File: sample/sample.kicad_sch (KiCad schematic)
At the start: 40 parts, among them M1 NMOS4pin, M2 PMOS4pin, M3 NMOS4pin, M4 PMOS4pin, M5 NMOS4pin, M6 PMOS4pin, M7 NMOS4pin, M8 NMOS4pin, M9 NMOS3pin_1, U1 GND_Drafting, U10 not, U11 V_{DD}, U12 D_FF_R, U13 nor21, U14 D_FF_R, U15 D_FF_R, U16 nor21, U17 D_FF_R, U18 D_FF_R, U19 OP_AMP, U2 V_{DD}, U20 delay, U21 OP_AMP, U22 RS_FF, U25 nand21, U3 V_{DD}, U4 GND_Drafting, U5 GND_Drafting, U6 GND_Drafting, U7 V_{DD}, U8 V_{DD}, U9 or31

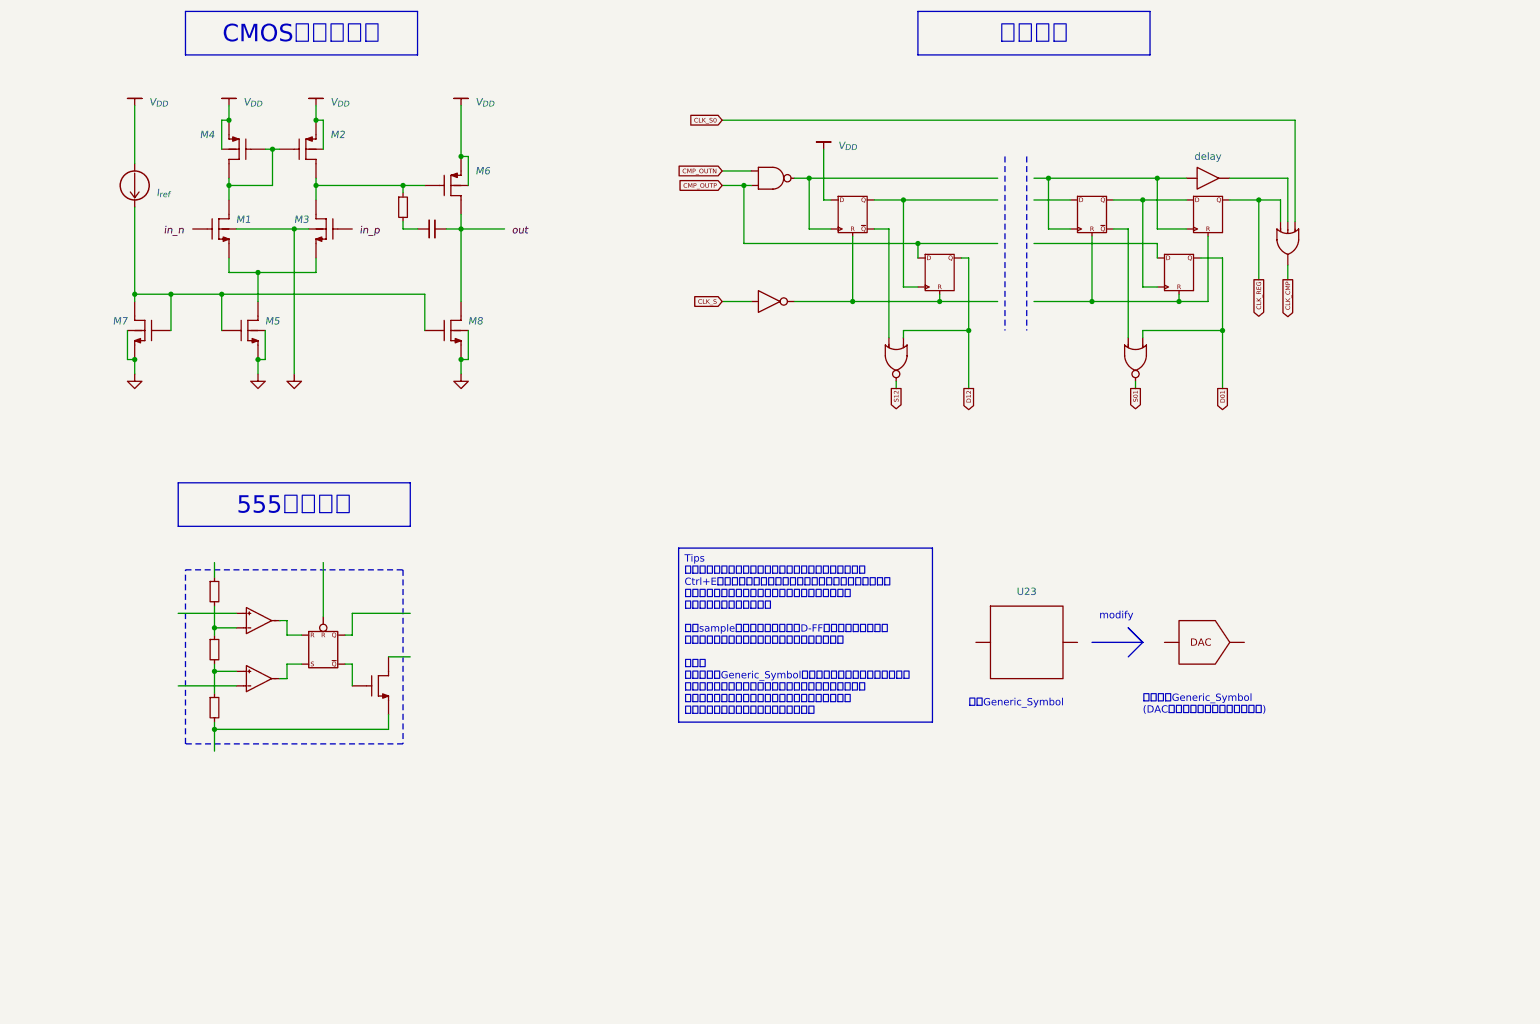
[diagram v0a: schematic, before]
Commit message: マルチプレクサの追加とサンプルの改修
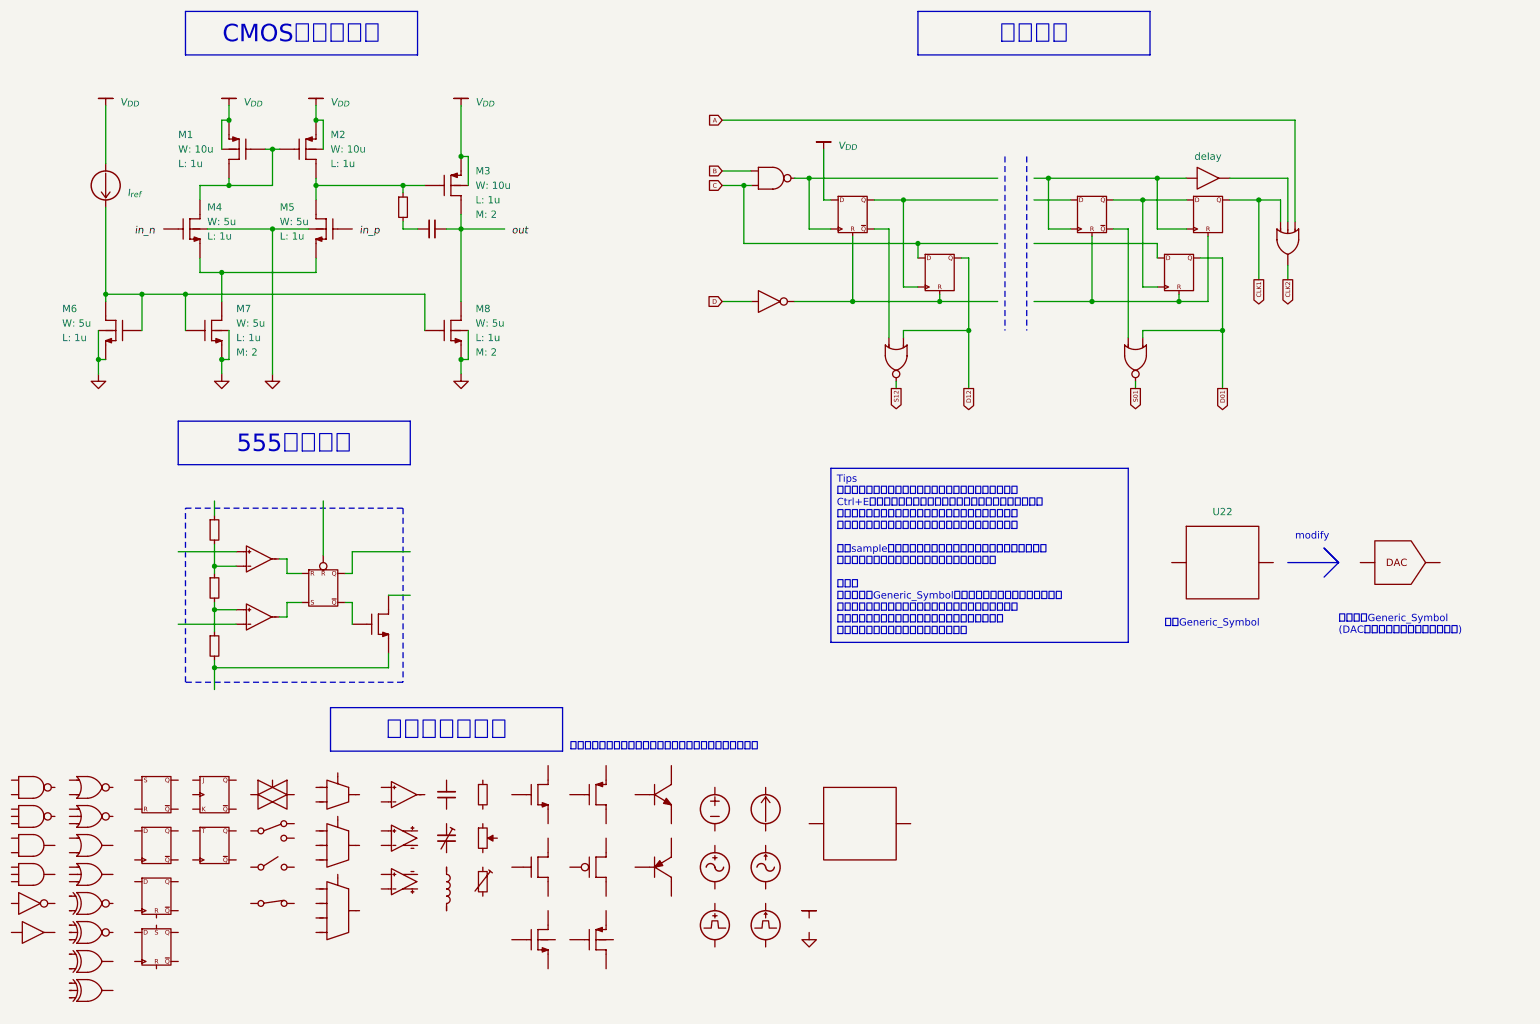
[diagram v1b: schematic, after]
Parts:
- removed M1, M3: NMOS4pin, symbol Drafting_Symbols:NMOS4pin
- removed M4, M6: PMOS4pin, symbol Drafting_Symbols:PMOS4pin
- added C2: C, symbol Drafting_Symbols:C_Drafting
- added C3: C_Trim, symbol Drafting_Symbols:C_Trim_Drafting
- added I_AC1: I_AC, symbol Drafting_Symbols:I_AC
- added I_DC2: I_DC, symbol Drafting_Symbols:I_DC
- added I_Pulse1: I_Pulse, symbol Drafting_Symbols:I_Pulse
- added L1: L, symbol Drafting_Symbols:L_Drafting
- added M1, M15, M3: PMOS4pin, symbol Drafting_Symbols:PMOS4pin
- added M10: NMOS3pin_1, symbol Drafting_Symbols:NMOS3pin_1
- added M11: PMOS3pin_1, symbol Drafting_Symbols:PMOS3pin_1
- added M12: NMOS3pin_2, symbol Drafting_Symbols:NMOS3pin_2
- added M13: PMOS3pin_2, symbol Drafting_Symbols:PMOS3pin_2
- added M14, M4, M6: NMOS4pin, symbol Drafting_Symbols:NMOS4pin
- added Q1: NPN, symbol Drafting_Symbols:NPN
- added Q2: PNP, symbol Drafting_Symbols:PNP
- added R5: R, symbol Drafting_Symbols:R_Drafting
- added R6: R, symbol Drafting_Symbols:R_Trim_Drafting
- added RV1: R_POT, symbol Drafting_Symbols:R_Potentiometer_Drafting
- added SW1: SW_CMOS, symbol Drafting_Symbols:SW_CMOS
- added SW2: SW_SPDT, symbol Drafting_Symbols:SW_SPDT
- added SW3: SW_SPST_OFF, symbol Drafting_Symbols:SW_SPST_OFF
- added SW4: SW_SPST_ON, symbol Drafting_Symbols:SW_SPST_ON
- added U26: nand21, symbol Drafting_Symbols:nand21
- added U27: nor21, symbol Drafting_Symbols:nor21
- added U28: RS_FF, symbol Drafting_Symbols:RS_FF
- added U29: JK_FF, symbol Drafting_Symbols:JK_FF
- added U30: MUX21, symbol Drafting_Symbols:MUX21
- added U31: OP_AMP, symbol Drafting_Symbols:OP_AMP
- added U32: nand31, symbol Drafting_Symbols:nand31
- added U33: nor31, symbol Drafting_Symbols:nor31
- added U34: ~, symbol Drafting_Symbols:Generic_Symbol
- added U35: Differential_AMP, symbol Drafting_Symbols:Differential_AMP_2
- added U36: and21, symbol Drafting_Symbols:and21
- added U37: or21, symbol Drafting_Symbols:or21
- added U38: D_FF, symbol Drafting_Symbols:D_FF
- added U39: T_FF, symbol Drafting_Symbols:T_FF
- added U40: MUX31, symbol Drafting_Symbols:MUX31
- added U41: and31, symbol Drafting_Symbols:and31
- added U42: or31, symbol Drafting_Symbols:or31
- added U43: Differential_AMP, symbol Drafting_Symbols:Differential_AMP_1
- added U44: D_FF_R, symbol Drafting_Symbols:D_FF_R
- added U45: not, symbol Drafting_Symbols:not
- added U46: xnor21, symbol Drafting_Symbols:xnor21
- added U47: MUX41, symbol Drafting_Symbols:MUX41
- added U48: VDD_Drafting, symbol Drafting_Symbols:VDD_Drafting
- added U49: buf, symbol Drafting_Symbols:buf
- added U50: xnor31, symbol Drafting_Symbols:xnor31
- added U51: GND_Drafting, symbol Drafting_Symbols:GND_Drafting
- added U52: D_FF_R_S, symbol Drafting_Symbols:D_FF_R_S
- added U53: xor21, symbol Drafting_Symbols:xor21
- added U54: xor31, symbol Drafting_Symbols:xor31
- added V_AC1: V_AC, symbol Drafting_Symbols:V_AC
- added V_DC1: V_DC, symbol Drafting_Symbols:V_DC
- added V_Pulse1: V_Pulse, symbol Drafting_Symbols:V_Pulse
- M2: L (none) -> 1u; W (none) -> 10u
- M5: L (none) -> 1u; W (none) -> 5u
- M7, M8: L (none) -> 1u; M (none) -> 2; W (none) -> 5u
- renumbered U8 to U1, U18 to U10, U9 to U11, U14 to U12, U17 to U13, U10 to U14, U16 to U15, U13 to U16, U5 to U17, U1 to U18, U4 to U19, U6 to U20, U19 to U21, U23 to U22, U24 to U23, U22 to U24, U21 to U25, U7 to U4, U11 to U5, U25 to U6, U20 to U7, U12 to U8, U15 to U9
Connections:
- net CLK_S0 is gone; now on net CLK2: U11.1 (Y)
- net CMP_OUTN is gone; now on net C: U6.1 (Y)
- net GND: now also M2.2 (S), M2.4 (B), M5.4 (B), M7.3 (S), M7.4 (B), M8.3 (S), M8.4 (B), M1.2 (S), M1.4 (B), M3.2 (S), M3.4 (B), M4.4 (B), M6.3 (S), M6.4 (B), U48.1 (GND), U51.1 (GND); no longer M2.1 (S), M5.1 (S), M7.1 (S), M8.1 (S)
- net at M2.1 (G): now also M1.1 (G), M1.3 (D), M4.2 (D)
- net at U24.1 (~Q): now also M9.1 (S)
- net at U25.1 (out): no longer U24.1 (~Q)
- net at U21.1 (out): no longer U24.1 (~Q)
- net at M9.1 (S): no longer U24.1 (~Q)
- net C: now reaches U6.1 (Y)
- net C: now also U12.1 (R); no longer U8.1 (~Q)
- net at R1.1: now also M2.3 (D), M5.2 (D), M3.1 (G); no longer M2.1 (S)
- net at C1.2: now also M8.2 (D), M3.3 (D); no longer M8.1 (S)
- net at U7.1 (Y): now also U10.1 (R), U9.1 (~Q); no longer U11.1 (Y)
- net at I_DC1.1, M7.1 (G), M8.1 (G): now also M6.1 (G), M6.2 (D); no longer M5.1 (S)
- net at U9.1 (~Q): now also U10.1 (R), U13.1 (R)
- net CLK_CMP renamed CLK2
- net CLK_REG renamed CLK1
- net CLK_S renamed D
- removed net CMP_OUTP: U12.1 (R), U6.1 (Y)
- new net: M4.3 (S), M5.3 (S), M7.2 (D)
- new net: U24.1 (~Q), U25.1 (out)
- new net: U21.1 (out), U24.1 (~Q)
- new net: U6.1 (Y), U8.1 (~Q)
- new net: U15.1 (Y), U8.1 (~Q)
- new net: U11.1 (Y), U7.1 (Y)
- new net: U12.1 (R), U14.1 (Y), U8.1 (~Q)
- new net: U16.1 (Y), U9.1 (~Q)
- new net: U10.1 (R), U13.1 (R), U9.1 (~Q)
- new net: U12.1 (R), U8.1 (~Q)
- new net A: U11.1 (Y)
- new net B: U6.1 (Y)
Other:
- note added: "最新版のシンボルはここに含まれていないことがあります"
- moved on the sheet: U22

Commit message: サンプルの修正
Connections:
- net at U24.1 (~Q): now also M9.1 (S)
- net at U25.1 (out): no longer U24.1 (~Q)
- net at U21.1 (out): no longer U24.1 (~Q)
- net at M9.1 (S): no longer U24.1 (~Q)
- net at U7.1 (Y): now also U10.1 (R), U9.1 (~Q); no longer U11.1 (Y)
- net at U9.1 (~Q): now also U10.1 (R), U13.1 (R)
- new net: U24.1 (~Q), U25.1 (out)
- new net: U21.1 (out), U24.1 (~Q)
- new net: U6.1 (Y), U8.1 (~Q)
- new net: U15.1 (Y), U8.1 (~Q)
- new net: U11.1 (Y), U7.1 (Y)
- new net: U12.1 (R), U14.1 (Y), U8.1 (~Q)
- new net: U16.1 (Y), U9.1 (~Q)
- new net: U10.1 (R), U13.1 (R), U9.1 (~Q)
- new net: U12.1 (R), U8.1 (~Q)
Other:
- moved on the sheet: M1
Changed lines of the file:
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@@
   (junction (at 220.98 71.12) (diameter 0) (color 0 0 0 0)
   )
-  (junction (at 54.61 39.37) (diameter 0) (color 0 0 0 0)
+  (junction (at 49.53 39.37) (diameter 0) (color 0 0 0 0)
+  )
+  (junction (at 58.42 44.45) (diameter 0) (color 0 0 0 0)
   )
   (junction (at 228.6 76.2) (diameter 0) (color 0 0 0 0)
@@
   (junction (at 33.02 69.85) (diameter 0) (color 0 0 0 0)
   )
-  (junction (at 62.23 44.45) (diameter 0) (color 0 0 0 0)
-  )
   (junction (at 85.09 50.8) (diameter 0) (color 0 0 0 0)
   )
@@
   (junction (at 95.25 58.42) (diameter 0) (color 0 0 0 0)
   )
-  (junction (at 54.61 50.8) (diameter 0) (color 0 0 0 0)
-  )
   (junction (at 52.07 125.095) (diameter 0) (color 0 0 0 0)
   )
@@
   (junction (at 172.72 53.34) (diameter 0) (color 0 0 0 0)
   )
+  (junction (at 49.53 50.8) (diameter 0) (color 0 0 0 0)
+  )
   (junction (at 62.23 58.42) (diameter 0) (color 0 0 0 0)
   )
@@
     (stroke (width 0) (type default))
   )
-  (wire (pts (xy 62.23 50.8) (xy 62.23 44.45))
+  (wire (pts (xy 58.42 50.8) (xy 58.42 44.45))
     (stroke (width 0) (type default))
   )
@@
   )
   (wire (pts (xy 53.34 83.82) (xy 53.34 81.28))
-    (stroke (width 0) (type default))
-  )
-  (wire (pts (xy 49.53 50.8) (xy 54.61 50.8))
     (stroke (width 0) (type default))
   )
@@
     (stroke (width 0) (type default))
   )
+  (wire (pts (xy 49.53 50.8) (xy 58.42 50.8))
+    (stroke (width 0) (type default))
+  )
   (wire (pts (xy 195.58 49.53) (xy 198.12 49.53))
     (stroke (width 0) (type default))
@@
     (stroke (width 0) (type default))
   )
-  (wire (pts (xy 53.34 39.37) (xy 54.61 39.37))
+  (wire (pts (xy 48.26 39.37) (xy 49.53 39.37))
     (stroke (width 0) (type default))
   )
@@
     (stroke (width 0) (type default))
   )
-  (wire (pts (xy 62.23 44.45) (xy 60.96 44.45))
-    (stroke (width 0) (type default))
-  )
-  (wire (pts (xy 54.61 36.83) (xy 54.61 39.37))
+  (wire (pts (xy 49.53 36.83) (xy 49.53 39.37))
     (stroke (width 0) (type default))
   )
@@
     (stroke (width 0) (type default))
   )
+  (wire (pts (xy 58.42 44.45) (xy 63.5 44.45))
+    (stroke (width 0) (type default))
+  )
   (wire (pts (xy 71.12 106.045) (xy 71.12 115.57))
     (stroke (width 0) (type default))
@@
     (stroke (width 0) (type default))
   )
-  (wire (pts (xy 53.34 44.45) (xy 53.34 39.37))
+  (wire (pts (xy 48.26 44.45) (xy 48.26 39.37))
     (stroke (width 0) (type default))
   )
@@
     (stroke (width 0) (type default))
   )
-  (wire (pts (xy 54.61 50.8) (xy 62.23 50.8))
-    (stroke (width 0) (type default))
-  )
-  (wire (pts (xy 62.23 44.45) (xy 63.5 44.45))
-    (stroke (width 0) (type default))
-  )
   (wire (pts (xy 39.37 69.85) (xy 46.99 69.85))
     (stroke (width 0) (type default))
@@
     (stroke (width 0) (type default))
   )
-  (wire (pts (xy 54.61 49.53) (xy 54.61 50.8))
+  (wire (pts (xy 49.53 49.53) (xy 49.53 50.8))
     (stroke (width 0) (type default))
   )
@@
   )
   (wire (pts (xy 49.53 63.5) (xy 49.53 66.04))
+    (stroke (width 0) (type default))
+  )
+  (wire (pts (xy 58.42 44.45) (xy 55.88 44.45))
     (stroke (width 0) (type default))
   )
@@
     )
   )
-  (symbol (lib_id "Drafting_Symbols:VDD_Drafting") (at 54.61 36.83 0) (unit 1)
-    (in_bom yes) (on_board yes) (dnp no) (fields_autoplaced)
-    (property "Reference" "U2" (at 54.61 34.29 0)
-      (effects (font (size 1.27 1.27)) hide)
-    )
-    (property "Value" "V_{DD}" (at 57.15 36.195 0)
+  (symbol (lib_id "Drafting_Symbols:VDD_Drafting") (at 49.53 36.83 0) (unit 1)
+    (in_bom yes) (on_board yes) (dnp no) (fields_autoplaced)
+    (property "Reference" "U2" (at 49.53 34.29 0)
+      (effects (font (size 1.27 1.27)) hide)
+    )
+    (property "Value" "V_{DD}" (at 52.07 36.195 0)
       (effects (font (size 1.27 1.27) italic) (justify left))
     )
-    (property "Footprint" "" (at 54.61 34.29 0)
-      (effects (font (size 1.27 1.27)) hide)
-    )
-    (property "Datasheet" "" (at 54.61 34.29 0)
+    (property "Footprint" "" (at 49.53 34.29 0)
+      (effects (font (size 1.27 1.27)) hide)
+    )
+    (property "Datasheet" "" (at 49.53 34.29 0)
       (effects (font (size 1.27 1.27)) hide)
     )
@@
     )
   )
-  (symbol (lib_name "PMOS4pin_1") (lib_id "Drafting_Symbols:PMOS4pin") (at 54.61 44.45 0) (mirror y) (unit 1)
+  (symbol (lib_name "PMOS4pin_1") (lib_id "Drafting_Symbols:PMOS4pin") (at 49.53 44.45 0) (mirror y) (unit 1)
     (in_bom yes) (on_board yes) (dnp no)
-    (property "Reference" "M1" (at 45.72 41.91 0)
+    (property "Reference" "M1" (at 40.64 41.91 0)
       (effects (font (size 1.27 1.27)) (justify right))
     )
-    (property "Value" "PMOS4pin" (at 55.88 38.1 0)
-      (effects (font (size 1.27 1.27)) hide)
-    )
-    (property "Footprint" "" (at 55.88 38.1 0)
-      (effects (font (size 1.27 1.27)) hide)
-    )
-    (property "Datasheet" "" (at 55.88 38.1 0)
-      (effects (font (size 1.27 1.27)) hide)
-    )
-    (property "W" "10u" (at 45.72 44.45 0) (show_name)
+    (property "Value" "PMOS4pin" (at 50.8 38.1 0)
+      (effects (font (size 1.27 1.27)) hide)
+    )
+    (property "Footprint" "" (at 50.8 38.1 0)
+      (effects (font (size 1.27 1.27)) hide)
+    )
+    (property "Datasheet" "" (at 50.8 38.1 0)
+      (effects (font (size 1.27 1.27)) hide)
+    )
+    (property "W" "10u" (at 40.64 44.45 0) (show_name)
       (effects (font (size 1.27 1.27)) (justify right))
     )
-    (property "L" "1u" (at 45.72 46.99 0) (show_name)
+    (property "L" "1u" (at 40.64 46.99 0) (show_name)
       (effects (font (size 1.27 1.27)) (justify right))
     )
-    (property "M" "" (at 54.61 44.45 0)
+    (property "M" "" (at 49.53 44.45 0)
       (effects (font (size 1.27 1.27)) (justify left))
     )

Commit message: kicad8
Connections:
- net at U24.1 (~Q): now also M9.1 (S)
- net at U25.1 (out): no longer U24.1 (~Q)
- net at U21.1 (out): no longer U24.1 (~Q)
- net at M9.1 (S): no longer U24.1 (~Q)
- net at U7.1 (Y): now also U10.1 (R), U9.1 (~Q); no longer U11.1 (Y)
- net at U9.1 (~Q): now also U10.1 (R), U13.1 (R)
- new net: U24.1 (~Q), U25.1 (out)
- new net: U21.1 (out), U24.1 (~Q)
- new net: U6.1 (Y), U8.1 (~Q)
- new net: U15.1 (Y), U8.1 (~Q)
- new net: U11.1 (Y), U7.1 (Y)
- new net: U12.1 (R), U14.1 (Y), U8.1 (~Q)
- new net: U16.1 (Y), U9.1 (~Q)
- new net: U10.1 (R), U13.1 (R), U9.1 (~Q)
- new net: U12.1 (R), U8.1 (~Q)
